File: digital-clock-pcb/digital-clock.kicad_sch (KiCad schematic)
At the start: 0 parts

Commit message: add pcb
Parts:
- added C1: C_Small, Capacitor_SMD:C_0603_1608Metric, symbol Device:C_Small
- added D1, D10, D11, D12, D13, D14, D15, D16, D17, D18, D19, D2, D20, D21, D3, D4, D5, D6, D7, D8, D9: WS2812B, LED_SMD:LED_WS2812B_PLCC4_5.0x5.0mm_P3.2mm, symbol LED:WS2812B
- added J1: USB_OTG, Connector_USB:USB_Micro-B_Molex-105017-0001, symbol Connector:USB_OTG
- added J2: Conn_02x03_Odd_Even, Connector_PinHeader_2.54mm:PinHeader_2x03_P2.54mm_Vertical, symbol Connector_Generic:Conn_02x03_Odd_Even
- added R1, R2: R_Small, Resistor_SMD:R_0603_1608Metric, symbol Device:R_Small
- added U1: ATmega328P-M, Package_DFN_QFN:QFN-32-1EP_5x5mm_P0.5mm_EP3.1x3.1mm, symbol MCU_Microchip_ATmega:ATmega328P-M
- added U2: PCF8523T, Package_SO:SOIC-8_3.9x4.9mm_P1.27mm, symbol Timer_RTC:PCF8523T
- added Y1: ABS2532768KHZ6T, Crystal:Crystal_SMD_Abracon_ABS25-4Pin_8.0x3.8mm, symbol ABS2532768KHZ6T:ABS2532768KHZ6T
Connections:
- new net: D17.2 (DOUT), D19.4 (DIN)
- new net: D17.4 (DIN), D20.2 (DOUT)
- new net: D15.2 (DOUT), D16.4 (DIN)
- new net: D10.2 (DOUT), D15.4 (DIN)
- new net: D12.4 (DIN), D7.2 (DOUT)
- new net: D2.2 (DOUT), D7.4 (DIN)
- new net: D11.4 (DIN), D6.2 (DOUT)
- new net: D1.2 (DOUT), D6.4 (DIN)
- new net: D16.2 (DOUT), D18.4 (DIN)
- new net: D10.4 (DIN), D5.2 (DOUT)
- new net: D11.2 (DOUT), D2.4 (DIN)
- new net: U2.1 (OSCI), Y1.1
- new net: Y1.2 (NC), Y1.3 (NC)
- new net: U2.2 (OSCO), Y1.4
- new net: D19.2 (DOUT), D21.4 (DIN)
- new net: D18.2 (DOUT), D20.4 (DIN)
- new net: D13.2 (DOUT), D4.4 (DIN)
- new net: D13.4 (DIN), D8.2 (DOUT)
- new net: D3.2 (DOUT), D8.4 (DIN)
- new net: D12.2 (DOUT), D3.4 (DIN)
- new net: D14.2 (DOUT), D5.4 (DIN)
- new net: D14.4 (DIN), D9.2 (DOUT)
- new net: D4.2 (DOUT), D9.4 (DIN)
- new net GND: C1.2, D1.3 (VSS), D10.3 (VSS), D11.3 (VSS), D12.3 (VSS), D13.3 (VSS), D14.3 (VSS), D15.3 (VSS), D16.3 (VSS), D17.3 (VSS), D18.3 (VSS), D19.3 (VSS), D2.3 (VSS), D20.3 (VSS), D21.3 (VSS), D3.3 (VSS), D4.3 (VSS), D5.3 (VSS), D6.3 (VSS), D7.3 (VSS), D8.3 (VSS), D9.3 (VSS), J1.5 (GND), J1.6 (Shield), J2.6 (Pin_6), U1.21 (GND), U1.3 (GND), U1.33 (GND), U1.5 (GND), U2.4 (VSS)
- new net MISO: J2.1 (Pin_1), U1.16 (PB4)
- new net MOSI: J2.4 (Pin_4), U1.15 (PB3)
- new net RST: J2.5 (Pin_5), U1.29 (~{RESET}/PC6)
- new net SCK: J2.3 (Pin_3), U1.17 (PB5)
- new net SCL: R2.2, U1.28 (PC5), U2.6 (SCL)
- new net SDA: R1.2, U1.27 (PC4), U2.5 (SDA)
- new net SS: U1.14 (PB2)
- new net VCC: C1.1, D1.1 (VDD), D10.1 (VDD), D11.1 (VDD), D12.1 (VDD), D13.1 (VDD), D14.1 (VDD), D15.1 (VDD), D16.1 (VDD), D17.1 (VDD), D18.1 (VDD), D19.1 (VDD), D2.1 (VDD), D20.1 (VDD), D21.1 (VDD), D3.1 (VDD), D4.1 (VDD), D5.1 (VDD), D6.1 (VDD), D7.1 (VDD), D8.1 (VDD), D9.1 (VDD), J1.1 (VBUS), J2.2 (Pin_2), R1.1, R2.1, U1.18 (AVCC), U1.4 (VCC), U1.6 (VCC), U2.8 (VDD)
- new net WS_IN: D1.4 (DIN), U1.13 (PB1)
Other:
- note added: "ATMEGA328P-M"
- note added: "ICSP"
- note added: "MICRO-USB"
- note added: "RTC PCF8523"
- note added: "WS2812"

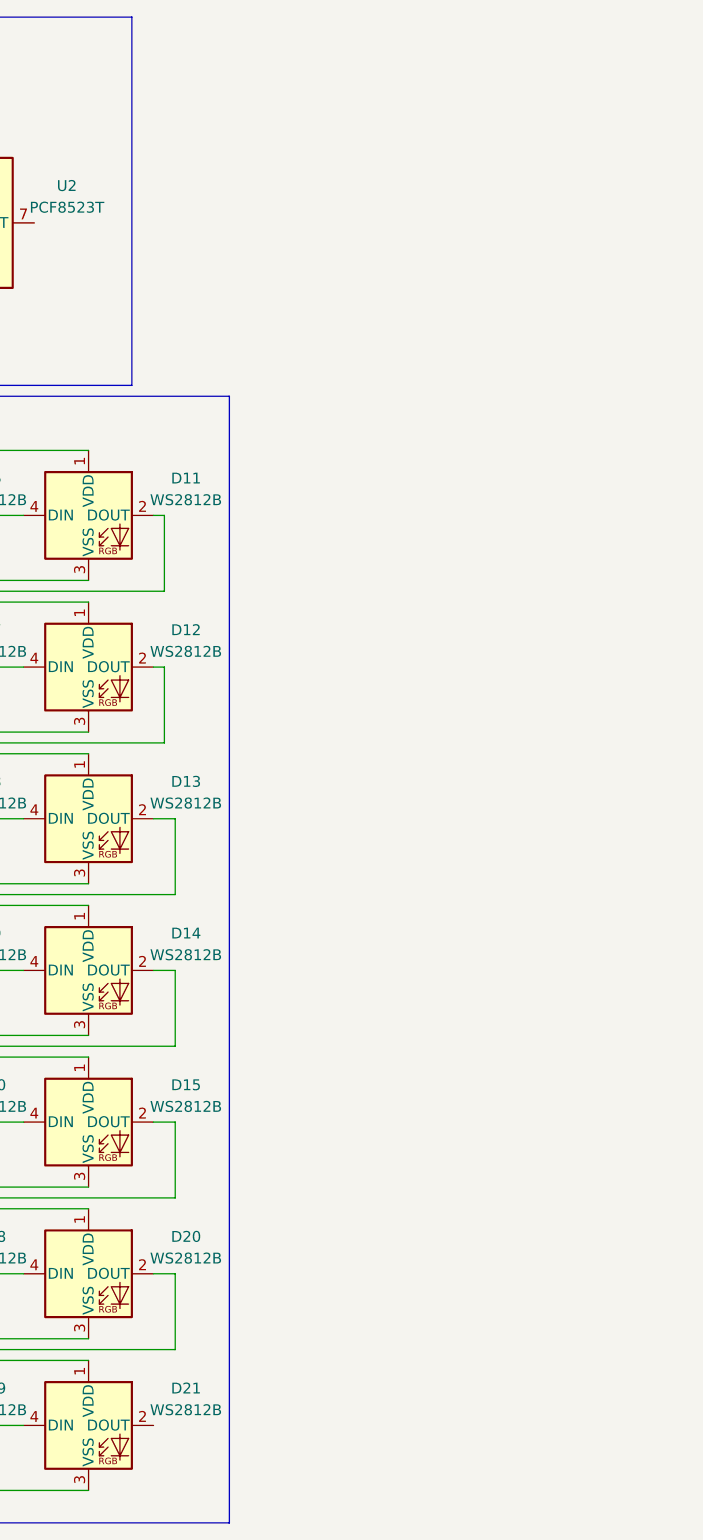
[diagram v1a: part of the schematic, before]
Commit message: add connector
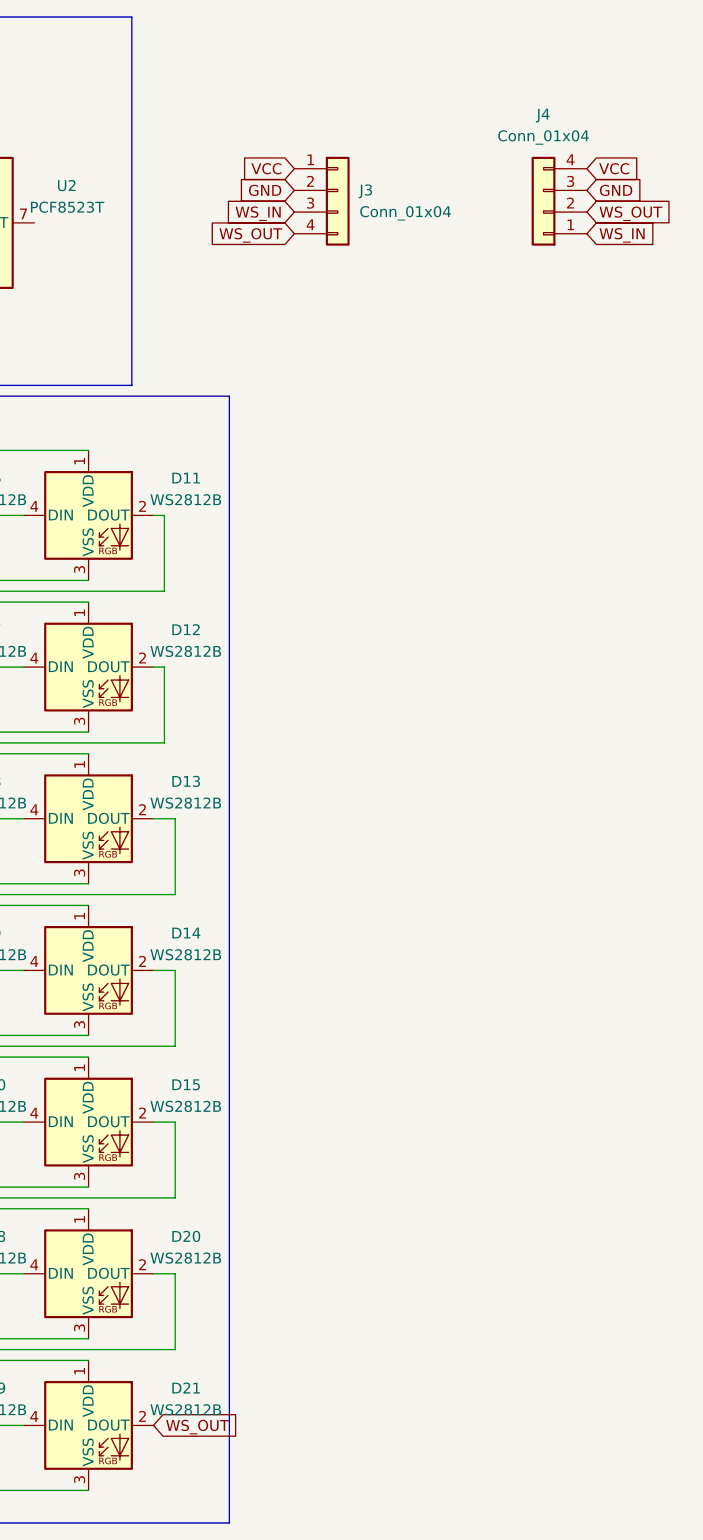
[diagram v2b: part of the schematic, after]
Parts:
- added J3, J4: Conn_01x04, Connector_JST:JST_SH_SM04B-SRSS-TB_1x04-1MP_P1.00mm_Horizontal, symbol Connector_Generic:Conn_01x04
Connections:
- net GND: now also J3.2 (Pin_2), J4.3 (Pin_3)
- net VCC: now also J3.1 (Pin_1), J4.4 (Pin_4)
- net WS_IN: now also J3.3 (Pin_3), J4.1 (Pin_1)
- net WS_OUT: now reaches D21.2 (DOUT)
- net WS_OUT: now also J3.4 (Pin_4), J4.2 (Pin_2)
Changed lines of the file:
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@@
+    )
+  )
+  (global_label "VCC" (shape input) (at 195.58 31.75 0) (fields_autoplaced)
+    (effects (font (size 1.27 1.27)) (justify left))
+    (property "Intersheet References" "${INTERSHEET_REFS}" (id 0) (at 201.6217 31.6706 0)
+      (effects (font (size 1.27 1.27)) (justify left) hide)
     )
   )
@@
     )
   )
+  (global_label "VCC" (shape input) (at 161.29 31.75 180) (fields_autoplaced)
+    (effects (font (size 1.27 1.27)) (justify right))
+    (property "Intersheet References" "${INTERSHEET_REFS}" (id 0) (at 155.2483 31.6706 0)
+      (effects (font (size 1.27 1.27)) (justify right) hide)
+    )
+  )
   (global_label "VCC" (shape input) (at 68.58 24.13 0) (fields_autoplaced)
     (effects (font (size 1.27 1.27)) (justify left))
@@
     )
   )
+  (global_label "WS_IN" (shape input) (at 195.58 39.37 0) (fields_autoplaced)
+    (effects (font (size 1.27 1.27)) (justify left))
+    (property "Intersheet References" "${INTERSHEET_REFS}" (id 0) (at 203.5569 39.2906 0)
+      (effects (font (size 1.27 1.27)) (justify left) hide)
+    )
+  )
   (global_label "GND" (shape input) (at 76.2 186.69 180) (fields_autoplaced)
     (effects (font (size 1.27 1.27)) (justify right))
@@
     )
   )
+  (global_label "WS_IN" (shape input) (at 161.29 36.83 180) (fields_autoplaced)
+    (effects (font (size 1.27 1.27)) (justify right))
+    (property "Intersheet References" "${INTERSHEET_REFS}" (id 0) (at 153.3131 36.7506 0)
+      (effects (font (size 1.27 1.27)) (justify right) hide)
+    )
+  )
   (global_label "SDA" (shape input) (at 50.8 101.6 0) (fields_autoplaced)
     (effects (font (size 1.27 1.27)) (justify left))
@@
     )
   )
+  (global_label "WS_OUT" (shape input) (at 195.58 36.83 0) (fields_autoplaced)
+    (effects (font (size 1.27 1.27)) (justify left))
+    (property "Intersheet References" "${INTERSHEET_REFS}" (id 0) (at 205.2502 36.7506 0)
+      (effects (font (size 1.27 1.27)) (justify left) hide)
+    )
+  )
+  (global_label "GND" (shape input) (at 161.29 34.29 180) (fields_autoplaced)
+    (effects (font (size 1.27 1.27)) (justify right))
+    (property "Intersheet References" "${INTERSHEET_REFS}" (id 0) (at 155.0064 34.2106 0)
+      (effects (font (size 1.27 1.27)) (justify right) hide)
+    )
+  )
   (global_label "MOSI" (shape input) (at 50.8 76.2 0) (fields_autoplaced)
     (effects (font (size 1.27 1.27)) (justify left))
@@
     )
   )
+  (global_label "WS_OUT" (shape input) (at 161.29 39.37 180) (fields_autoplaced)
+    (effects (font (size 1.27 1.27)) (justify right))
+    (property "Intersheet References" "${INTERSHEET_REFS}" (id 0) (at 151.6198 39.2906 0)
+      (effects (font (size 1.27 1.27)) (justify right) hide)
+    )
+  )
   (global_label "VCC" (shape input) (at 93.98 19.05 180) (fields_autoplaced)
     (effects (font (size 1.27 1.27)) (justify right))
@@
     (effects (font (size 1.27 1.27)) (justify left))
     (property "Intersheet References" "${INTERSHEET_REFS}" (id 0) (at 56.6602 106.6006 0)
+      (effects (font (size 1.27 1.27)) (justify left) hide)
+    )
+  )
+  (global_label "WS_OUT" (shape input) (at 144.78 179.07 0) (fields_autoplaced)
+    (effects (font (size 1.27 1.27)) (justify left))
+    (property "Intersheet References" "${INTERSHEET_REFS}" (id 0) (at 154.4502 178.9906 0)
+      (effects (font (size 1.27 1.27)) (justify left) hide)
+    )
+  )
+  (global_label "GND" (shape input) (at 195.58 34.29 0) (fields_autoplaced)
+    (effects (font (size 1.27 1.27)) (justify left))
+    (property "Intersheet References" "${INTERSHEET_REFS}" (id 0) (at 201.8636 34.2106 0)
       (effects (font (size 1.27 1.27)) (justify left) hide)
     )
@@
     (pin "4")
   )
+  (symbol (lib_id "Connector_Generic:Conn_01x04") (at 166.37 34.29 0) (unit 1)
+    (in_bom yes) (on_board yes) (fields_autoplaced)
+    (property "Reference" "J3" (id 0) (at 168.91 34.2899 0)
+      (effects (font (size 1.27 1.27)) (justify left))
+    )
+    (property "Value" "Conn_01x04" (id 1) (at 168.91 36.8299 0)
+      (effects (font (size 1.27 1.27)) (justify left))
+    )
+    (property "Footprint" "Connector_JST:JST_SH_SM04B-SRSS-TB_1x04-1MP_P1.00mm_Horizontal" (id 2) (at 166.37 34.29 0)
+      (effects (font (size 1.27 1.27)) hide)
+    )
+    (property "Datasheet" "~" (id 3) (at 166.37 34.29 0)
+      (effects (font (size 1.27 1.27)) hide)
+    )
+    (pin "1")
+    (pin "2")
+    (pin "3")
+    (pin "4")
+  )
   (symbol (lib_id "Device:R_Small") (at 96.52 24.13 0) (unit 1)
     (in_bom yes) (on_board yes)
@@
     (property "Datasheet" "https://cdn-shop.adafruit.com/datasheets/WS2812B.pdf" (id 3) (at 93.98 153.035 0)
       (effects (font (size 1.27 1.27)) (justify left top) hide)
+    )
+    (pin "1")
+    (pin "2")
+    (pin "3")
+    (pin "4")
+  )
+  (symbol (lib_id "Connector_Generic:Conn_01x04") (at 190.5 36.83 180) (unit 1)
+    (in_bom yes) (on_board yes) (fields_autoplaced)
+    (property "Reference" "J4" (id 0) (at 190.5 25.4 0))
+    (property "Value" "Conn_01x04" (id 1) (at 190.5 27.94 0))
+    (property "Footprint" "Connector_JST:JST_SH_SM04B-SRSS-TB_1x04-1MP_P1.00mm_Horizontal" (id 2) (at 190.5 36.83 0)
+      (effects (font (size 1.27 1.27)) hide)
+    )
+    (property "Datasheet" "~" (id 3) (at 190.5 36.83 0)
+      (effects (font (size 1.27 1.27)) hide)
     )
     (pin "1")
@@
       (reference "J2") (unit 1) (value "Conn_02x03_Odd_Even") (footprint "Connector_PinHeader_2.54mm:PinHeader_2x03_P2.54mm_Vertical")
     )
+    (path "/a442b559-9491-4fe0-a034-d4b1ca7c33fd"
+      (reference "J3") (unit 1) (value "Conn_01x04") (footprint "Connector_JST:JST_SH_SM04B-SRSS-TB_1x04-1MP_P1.00mm_Horizontal")
+    )
+    (path "/c4c7a3ca-a623-46c2-9315-d8549deeec27"
+      (reference "J4") (unit 1) (value "Conn_01x04") (footprint "Connector_JST:JST_SH_SM04B-SRSS-TB_1x04-1MP_P1.00mm_Horizontal")
+    )
     (path "/a94b0acc-5ec4-4bc9-978d-29de1f7738b5"

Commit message: wiring connector
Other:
- note added: "IN CONNECTOR"
- note added: "OUT CONNECTOR"
- moved on the sheet: J3, J4
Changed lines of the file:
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@@
+    (stroke (width 0) (type default) (color 0 0 0 0))
+  )
+  (polyline (pts (xy 144.78 34.29) (xy 144.78 55.88))
     (stroke (width 0) (type default) (color 0 0 0 0))
   )
@@
     (stroke (width 0) (type default) (color 0 0 0 0))
   )
+  (polyline (pts (xy 144.78 34.29) (xy 180.34 34.29))
+    (stroke (width 0) (type default) (color 0 0 0 0))
+  )
   (wire (pts (xy 78.74 115.57) (xy 78.74 133.35))
     (stroke (width 0) (type default) (color 0 0 0 0))
   )
+  (polyline (pts (xy 180.34 33.02) (xy 144.78 33.02))
+    (stroke (width 0) (type default) (color 0 0 0 0))
+  )
   (wire (pts (xy 144.78 72.39) (xy 146.05 72.39))
     (stroke (width 0) (type default) (color 0 0 0 0))
@@
     (stroke (width 0) (type default) (color 0 0 0 0))
   )
+  (polyline (pts (xy 144.78 13.97) (xy 144.78 33.02))
+    (stroke (width 0) (type default) (color 0 0 0 0))
+  )
   (wire (pts (xy 93.98 33.02) (xy 99.06 33.02))
     (stroke (width 0) (type default) (color 0 0 0 0))
@@
     (stroke (width 0) (type default) (color 0 0 0 0))
   )
+  (polyline (pts (xy 144.78 13.97) (xy 180.34 13.97))
+    (stroke (width 0) (type default) (color 0 0 0 0))
+  )
   (wire (pts (xy 147.32 170.18) (xy 81.28 170.18))
     (stroke (width 0) (type default) (color 0 0 0 0))
@@
     (stroke (width 0) (type default) (color 0 0 0 0))
   )
+  (polyline (pts (xy 180.34 13.97) (xy 180.34 33.02))
+    (stroke (width 0) (type default) (color 0 0 0 0))
+  )
   (polyline (pts (xy 142.24 13.97) (xy 81.28 13.97))
     (stroke (width 0) (type default) (color 0 0 0 0))
@@
     (stroke (width 0) (type default) (color 0 0 0 0))
   )
+  (polyline (pts (xy 180.34 34.29) (xy 180.34 55.88))
+    (stroke (width 0) (type default) (color 0 0 0 0))
+  )
   (wire (pts (xy 91.44 135.89) (xy 73.66 135.89))
     (stroke (width 0) (type default) (color 0 0 0 0))
@@
     (stroke (width 0) (type default) (color 0 0 0 0))
   )
+  (polyline (pts (xy 180.34 55.88) (xy 144.78 55.88))
+    (stroke (width 0) (type default) (color 0 0 0 0))
+  )
   (wire (pts (xy 78.74 133.35) (xy 78.74 151.13))
     (stroke (width 0) (type default) (color 0 0 0 0))
@@
   (wire (pts (xy 83.82 46.99) (xy 83.82 40.64))
     (stroke (width 0) (type default) (color 0 0 0 0))
+  )
+  (text "IN CONNECTOR" (at 144.78 16.51 0)
+    (effects (font (size 1.27 1.27)) (justify left bottom))
+  )
+  (text "OUT CONNECTOR" (at 146.05 36.83 0)
+    (effects (font (size 1.27 1.27)) (justify left bottom))
   )
   (text "RTC PCF8523" (at 81.28 16.51 0)
@@
     )
   )
-  (global_label "VCC" (shape input) (at 195.58 31.75 0) (fields_autoplaced)
-    (effects (font (size 1.27 1.27)) (justify left))
-    (property "Intersheet References" "${INTERSHEET_REFS}" (id 0) (at 201.6217 31.6706 0)
-      (effects (font (size 1.27 1.27)) (justify left) hide)
+  (global_label "VCC" (shape input) (at 161.29 53.34 180) (fields_autoplaced)
+    (effects (font (size 1.27 1.27)) (justify right))
+    (property "Intersheet References" "${INTERSHEET_REFS}" (id 0) (at 155.2483 53.4194 0)
+      (effects (font (size 1.27 1.27)) (justify right) hide)
     )
   )
@@
     )
   )
-  (global_label "VCC" (shape input) (at 161.29 31.75 180) (fields_autoplaced)
-    (effects (font (size 1.27 1.27)) (justify right))
-    (property "Intersheet References" "${INTERSHEET_REFS}" (id 0) (at 155.2483 31.6706 0)
+  (global_label "VCC" (shape input) (at 161.29 22.86 180) (fields_autoplaced)
+    (effects (font (size 1.27 1.27)) (justify right))
+    (property "Intersheet References" "${INTERSHEET_REFS}" (id 0) (at 155.2483 22.7806 0)
       (effects (font (size 1.27 1.27)) (justify right) hide)
     )
@@
     )
   )
-  (global_label "WS_IN" (shape input) (at 195.58 39.37 0) (fields_autoplaced)
-    (effects (font (size 1.27 1.27)) (justify left))
-    (property "Intersheet References" "${INTERSHEET_REFS}" (id 0) (at 203.5569 39.2906 0)
-      (effects (font (size 1.27 1.27)) (justify left) hide)
+  (global_label "WS_IN" (shape input) (at 161.29 45.72 180) (fields_autoplaced)
+    (effects (font (size 1.27 1.27)) (justify right))
+    (property "Intersheet References" "${INTERSHEET_REFS}" (id 0) (at 153.3131 45.7994 0)
+      (effects (font (size 1.27 1.27)) (justify right) hide)
     )
   )
@@
     )
   )
-  (global_label "WS_IN" (shape input) (at 161.29 36.83 180) (fields_autoplaced)
-    (effects (font (size 1.27 1.27)) (justify right))
-    (property "Intersheet References" "${INTERSHEET_REFS}" (id 0) (at 153.3131 36.7506 0)
+  (global_label "WS_IN" (shape input) (at 161.29 27.94 180) (fields_autoplaced)
+    (effects (font (size 1.27 1.27)) (justify right))
+    (property "Intersheet References" "${INTERSHEET_REFS}" (id 0) (at 153.3131 27.8606 0)
       (effects (font (size 1.27 1.27)) (justify right) hide)
     )
@@
     )
   )
-  (global_label "WS_OUT" (shape input) (at 195.58 36.83 0) (fields_autoplaced)
-    (effects (font (size 1.27 1.27)) (justify left))
-    (property "Intersheet References" "${INTERSHEET_REFS}" (id 0) (at 205.2502 36.7506 0)
-      (effects (font (size 1.27 1.27)) (justify left) hide)
-    )
-  )
-  (global_label "GND" (shape input) (at 161.29 34.29 180) (fields_autoplaced)
-    (effects (font (size 1.27 1.27)) (justify right))
-    (property "Intersheet References" "${INTERSHEET_REFS}" (id 0) (at 155.0064 34.2106 0)
+  (global_label "WS_OUT" (shape input) (at 161.29 48.26 180) (fields_autoplaced)
+    (effects (font (size 1.27 1.27)) (justify right))
+    (property "Intersheet References" "${INTERSHEET_REFS}" (id 0) (at 151.6198 48.3394 0)
+      (effects (font (size 1.27 1.27)) (justify right) hide)
+    )
+  )
+  (global_label "GND" (shape input) (at 161.29 25.4 180) (fields_autoplaced)
+    (effects (font (size 1.27 1.27)) (justify right))
+    (property "Intersheet References" "${INTERSHEET_REFS}" (id 0) (at 155.0064 25.3206 0)
       (effects (font (size 1.27 1.27)) (justify right) hide)
     )
@@
     )
   )
-  (global_label "WS_OUT" (shape input) (at 161.29 39.37 180) (fields_autoplaced)
-    (effects (font (size 1.27 1.27)) (justify right))
-    (property "Intersheet References" "${INTERSHEET_REFS}" (id 0) (at 151.6198 39.2906 0)
+  (global_label "WS_OUT" (shape input) (at 161.29 30.48 180) (fields_autoplaced)
+    (effects (font (size 1.27 1.27)) (justify right))
+    (property "Intersheet References" "${INTERSHEET_REFS}" (id 0) (at 151.6198 30.4006 0)
       (effects (font (size 1.27 1.27)) (justify right) hide)
     )
@@
     )
   )
-  (global_label "GND" (shape input) (at 195.58 34.29 0) (fields_autoplaced)
-    (effects (font (size 1.27 1.27)) (justify left))
-    (property "Intersheet References" "${INTERSHEET_REFS}" (id 0) (at 201.8636 34.2106 0)
-      (effects (font (size 1.27 1.27)) (justify left) hide)
+  (global_label "GND" (shape input) (at 161.29 50.8 180) (fields_autoplaced)
+    (effects (font (size 1.27 1.27)) (justify right))
+    (property "Intersheet References" "${INTERSHEET_REFS}" (id 0) (at 155.0064 50.8794 0)
+      (effects (font (size 1.27 1.27)) (justify right) hide)
     )
   )
@@
     (pin "4")
   )
-  (symbol (lib_id "Connector_Generic:Conn_01x04") (at 166.37 34.29 0) (unit 1)
-    (in_bom yes) (on_board yes) (fields_autoplaced)
-    (property "Reference" "J3" (id 0) (at 168.91 34.2899 0)
+  (symbol (lib_id "Connector_Generic:Conn_01x04") (at 166.37 25.4 0) (unit 1)
+    (in_bom yes) (on_board yes) (fields_autoplaced)
+    (property "Reference" "J3" (id 0) (at 168.91 25.3999 0)
       (effects (font (size 1.27 1.27)) (justify left))
     )
-    (property "Value" "Conn_01x04" (id 1) (at 168.91 36.8299 0)
+    (property "Value" "Conn_01x04" (id 1) (at 168.91 27.9399 0)
       (effects (font (size 1.27 1.27)) (justify left))
     )
-    (property "Footprint" "Connector_JST:JST_SH_SM04B-SRSS-TB_1x04-1MP_P1.00mm_Horizontal" (id 2) (at 166.37 34.29 0)
+    (property "Footprint" "Connector_JST:JST_SH_SM04B-SRSS-TB_1x04-1MP_P1.00mm_Horizontal" (id 2) (at 166.37 25.4 0)
       (effects (font (size 1.27 1.27)) hide)
     )
-    (property "Datasheet" "~" (id 3) (at 166.37 34.29 0)
+    (property "Datasheet" "~" (id 3) (at 166.37 25.4 0)
       (effects (font (size 1.27 1.27)) hide)
     )
@@
     (pin "4")
   )
-  (symbol (lib_id "Connector_Generic:Conn_01x04") (at 190.5 36.83 180) (unit 1)
-    (in_bom yes) (on_board yes) (fields_autoplaced)
-    (property "Reference" "J4" (id 0) (at 190.5 25.4 0))
-    (property "Value" "Conn_01x04" (id 1) (at 190.5 27.94 0))
-    (property "Footprint" "Connector_JST:JST_SH_SM04B-SRSS-TB_1x04-1MP_P1.00mm_Horizontal" (id 2) (at 190.5 36.83 0)
+  (symbol (lib_id "Connector_Generic:Conn_01x04") (at 166.37 48.26 0) (unit 1)
+    (in_bom yes) (on_board yes)
+    (property "Reference" "J4" (id 0) (at 170.18 50.8 0))
+    (property "Value" "Conn_01x04" (id 1) (at 173.99 48.26 0))
+    (property "Footprint" "Connector_JST:JST_SH_SM04B-SRSS-TB_1x04-1MP_P1.00mm_Horizontal" (id 2) (at 166.37 48.26 0)
       (effects (font (size 1.27 1.27)) hide)
     )
-    (property "Datasheet" "~" (id 3) (at 190.5 36.83 0)
+    (property "Datasheet" "~" (id 3) (at 166.37 48.26 0)
       (effects (font (size 1.27 1.27)) hide)
     )
